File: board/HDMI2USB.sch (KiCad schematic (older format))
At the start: 0 parts

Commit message: Issue #1481 - GPIO sheet
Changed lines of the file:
@@
 LIBS:valves
 LIBS:hdmi2usb
+LIBS:timvideos-pcie-8x
 LIBS:HDMI2USB-cache
-LIBS:Atlys-VHDCI-cache
 EELAYER 27 0
 EELAYER END
@@
 Sheet 1 12
 Title "HDMI2USB"
-Date "18 feb 2015"
+Date "20 feb 2015"
 Rev "Rev2"
 Comp ""
@@
 F38 "USB_RESETB" B R 5700 5950 60
 F39 "USB_REFCLK" B R 5700 5850 60
-$EndSheet
-$Sheet
-S 6550 1100 2000 2400
-U 54886DFB
-F0 "Ethernet" 50
-F1 "Ethernet.sch" 50
-F2 "ETH_TXD[0..3]" I R 8550 1500 60
-F3 "ETH_TXCTL" I R 8550 1700 60
-F4 "ETH_RXD[0..3]" I R 8550 1600 60
-F5 "ETH_TXCLK" I R 8550 1800 60
-F6 "ETH_RXCTL" I R 8550 1900 60
-F7 "ETH_RXCLK" I R 8550 2000 60
-F8 "ETH_INT_B" I R 8550 2100 60
-F9 "ETH_RESET_B" I R 8550 2200 60
-F10 "SYSCLK" I R 8550 2300 60
-F11 "FPGA_CLK" I R 8550 2400 60
-F12 "ETH_MDC" I R 8550 2500 60
-F13 "MAC_SCL" I R 8550 2800 60
-F14 "ETH_MDIO" I R 8550 2600 60
-F15 "MAC_SDA" I R 8550 2700 60
 $EndSheet
 $Sheet
@@
 	8550 2200 9800 2200
 Wire Wire Line
-	8550 2300 9800 2300
-Wire Wire Line
 	8550 2400 9800 2400
 Wire Wire Line
@@
 Wire Wire Line
 	8550 2600 9800 2600
-Wire Wire Line
-	8550 2700 9800 2700
 Wire Bus Line
 	3400 4300 3750 4300
@@
 Wire Bus Line
 	8550 4150 9800 4150
+$Sheet
+S 6550 1100 2000 2400
+U 54886DFB
+F0 "Ethernet" 50
+F1 "Ethernet.sch" 50
+F2 "ETH_TXD[0..3]" O R 8550 1500 60
+F3 "ETH_TXCTL" O R 8550 1700 60
+F4 "ETH_RXD[0..3]" I R 8550 1600 60
+F5 "ETH_TXCLK" O R 8550 1800 60
+F6 "ETH_RXCTL" I R 8550 1900 60
+F7 "ETH_RXCLK" I R 8550 2000 60
+F8 "ETH_INT_B" I R 8550 2100 60
+F9 "ETH_RESET_B" I R 8550 2200 60
+F10 "FPGA_CLK" I R 8550 2400 60
+F11 "ETH_MDC" I R 8550 2500 60
+F12 "MAC_SCL" I R 8550 2700 60
+F13 "ETH_MDIO" B R 8550 2600 60
+F14 "MAC_SDA" B R 8550 2800 60
+$EndSheet
 $Sheet
 S 9800 1100 2050 8900
@@
 F68 "CYPRESS-RESET" B L 9800 6400 60
 F69 "GTP_CLK" O L 9800 6500 60
-F70 "RX_CLK" O L 9800 3150 60
-F71 "ETH_RXCTL" I L 9800 1900 60
-F72 "ETH_RXCLK" I L 9800 2000 60
-F73 "ETH_RXD[0..3]" I L 9800 1600 60
-F74 "ETH_MDC" I L 9800 2500 60
-F75 "ETH_MDIO" I L 9800 2600 60
-F76 "ETH_RESET_B" I L 9800 2200 60
-F77 "ETH_INT_B" I L 9800 2100 60
-F78 "ETH_TXCLK" I L 9800 1800 60
-F79 "ETH_TXCTL" I L 9800 1700 60
-F80 "ETH_TXD[0..3]" I L 9800 1500 60
-F81 "FPGA_CLK" I L 9800 2400 60
-F82 "MAC_SCL" I L 9800 2800 60
-F83 "MAC_SDA" I L 9800 2700 60
-F84 "SYSCLK" I L 9800 2300 60
-$EndSheet
-$Sheet
-S 1900 7250 1450 2350
+F70 "ETH_RXCTL" O L 9800 1900 60
+F71 "ETH_RXCLK" O L 9800 2000 60
+F72 "ETH_RXD[0..3]" O L 9800 1600 60
+F73 "ETH_MDC" O L 9800 2500 60
+F74 "ETH_MDIO" B L 9800 2600 60
+F75 "ETH_RESET_B" O L 9800 2200 60
+F76 "ETH_INT_B" O L 9800 2100 60
+F77 "ETH_TXCLK" I L 9800 1800 60
+F78 "ETH_TXCTL" I L 9800 1700 60
+F79 "ETH_TXD[0..3]" I L 9800 1500 60
+F80 "FPGA_CLK" O L 9800 2400 60
+F81 "MAC_SCL" I L 9800 2700 60
+F82 "MAC_SDA" B L 9800 2800 60
+$EndSheet
+Wire Wire Line
+	9800 2800 8550 2800
+Wire Wire Line
+	8550 2700 9800 2700
+$Sheet
+S 1950 7250 1650 3400
 U 54E594A7
 F0 "GPIOs" 50
 F1 "GPIOs.sch" 50
+F2 "DIFFIO_A1N" B R 3600 7650 60
+F3 "DIFFIO_A2N" B R 3600 7850 60
+F4 "DIFFIO_A3N" B R 3600 8050 60
+F5 "DIFFCLK_A0N" B R 3600 9050 60
+F6 "DIFFIO_A4N" B R 3600 8250 60
+F7 "DIFFIO_A5N" B R 3600 8450 60
+F8 "DIFFIO_A6N" B R 3600 8650 60
+F9 "DIFFCLK_A1N" B R 3600 9300 60
+F10 "DIFFIO_B1N" B L 1950 7650 60
+F11 "DIFFIO_B2N" B L 1950 7850 60
+F12 "DIFFIO_B3N" B L 1950 8050 60
+F13 "DIFFCLK_B0N" B L 1950 9050 60
+F14 "DIFFIO_B4N" B L 1950 8250 60
+F15 "DIFFIO_B0N" B L 1950 7450 60
+F16 "DIFFIO_B6N" B L 1950 8650 60
+F17 "DIFFCLK_B1N" I L 1950 9300 60
+F18 "DIFFCLK_A1P" I R 3600 8950 60
+F19 "DIFFIO_A1P" B R 3600 7550 60
+F20 "DIFFIO_A2P" B R 3600 7750 60
+F21 "DIFFIO_A3P" B R 3600 7950 60
+F22 "DIFFCLK_A0P" B R 3600 9200 60
+F23 "DIFFIO_A4P" B R 3600 8150 60
+F24 "DIFFIO_A5P" B R 3600 8350 60
+F25 "DIFFIO_A6P" B R 3600 8550 60
+F26 "DIFFIO_B1P" B L 1950 7550 60
+F27 "DIFFIO_B2P" B L 1950 7750 60
+F28 "DIFFIO_B3P" B L 1950 7950 60
+F29 "DIFFCLK_B0P" B L 1950 8950 60
+F30 "DIFFIO_B4P" B L 1950 8150 60
+F31 "DIFFIO_B5P" B L 1950 8350 60
+F32 "DIFFIO_B6P" B L 1950 8550 60
+F33 "DIFFCLK_B1P" I L 1950 9200 60
+F34 "SMCLK" I L 1950 9450 60
+F35 "SMDATA" B L 1950 9550 60
+F36 "PCIE_RESET" I L 1950 9650 60
+F37 "DIFFIO_XP" B R 3600 9550 60
+F38 "DIFFIO_XN" B R 3600 9650 60
+F39 "DIFFIO_YN" B R 3600 9850 60
+F40 "DIFFIO_YP" B R 3600 9750 60
+F41 "DIFFCLK_XN" B R 3600 10250 60
+F42 "DIFFCLK_XP" B R 3600 10150 60
+F43 "DIFFIO_A0N" B R 3600 7450 60
+F44 "DIFFIO_A0P" B R 3600 7350 60
+F45 "DIFFIO_B0P" B L 1950 7350 60
+F46 "DIFFIO_ZN" B R 3600 10050 60
+F47 "DIFFIO_ZP" B R 3600 9950 60
+F48 "GPIO[0..15]" B L 1950 9900 60
+F49 "DIFFIO_B5N" B L 1950 8450 60
 $EndSheet
 $EndSCHEMATC

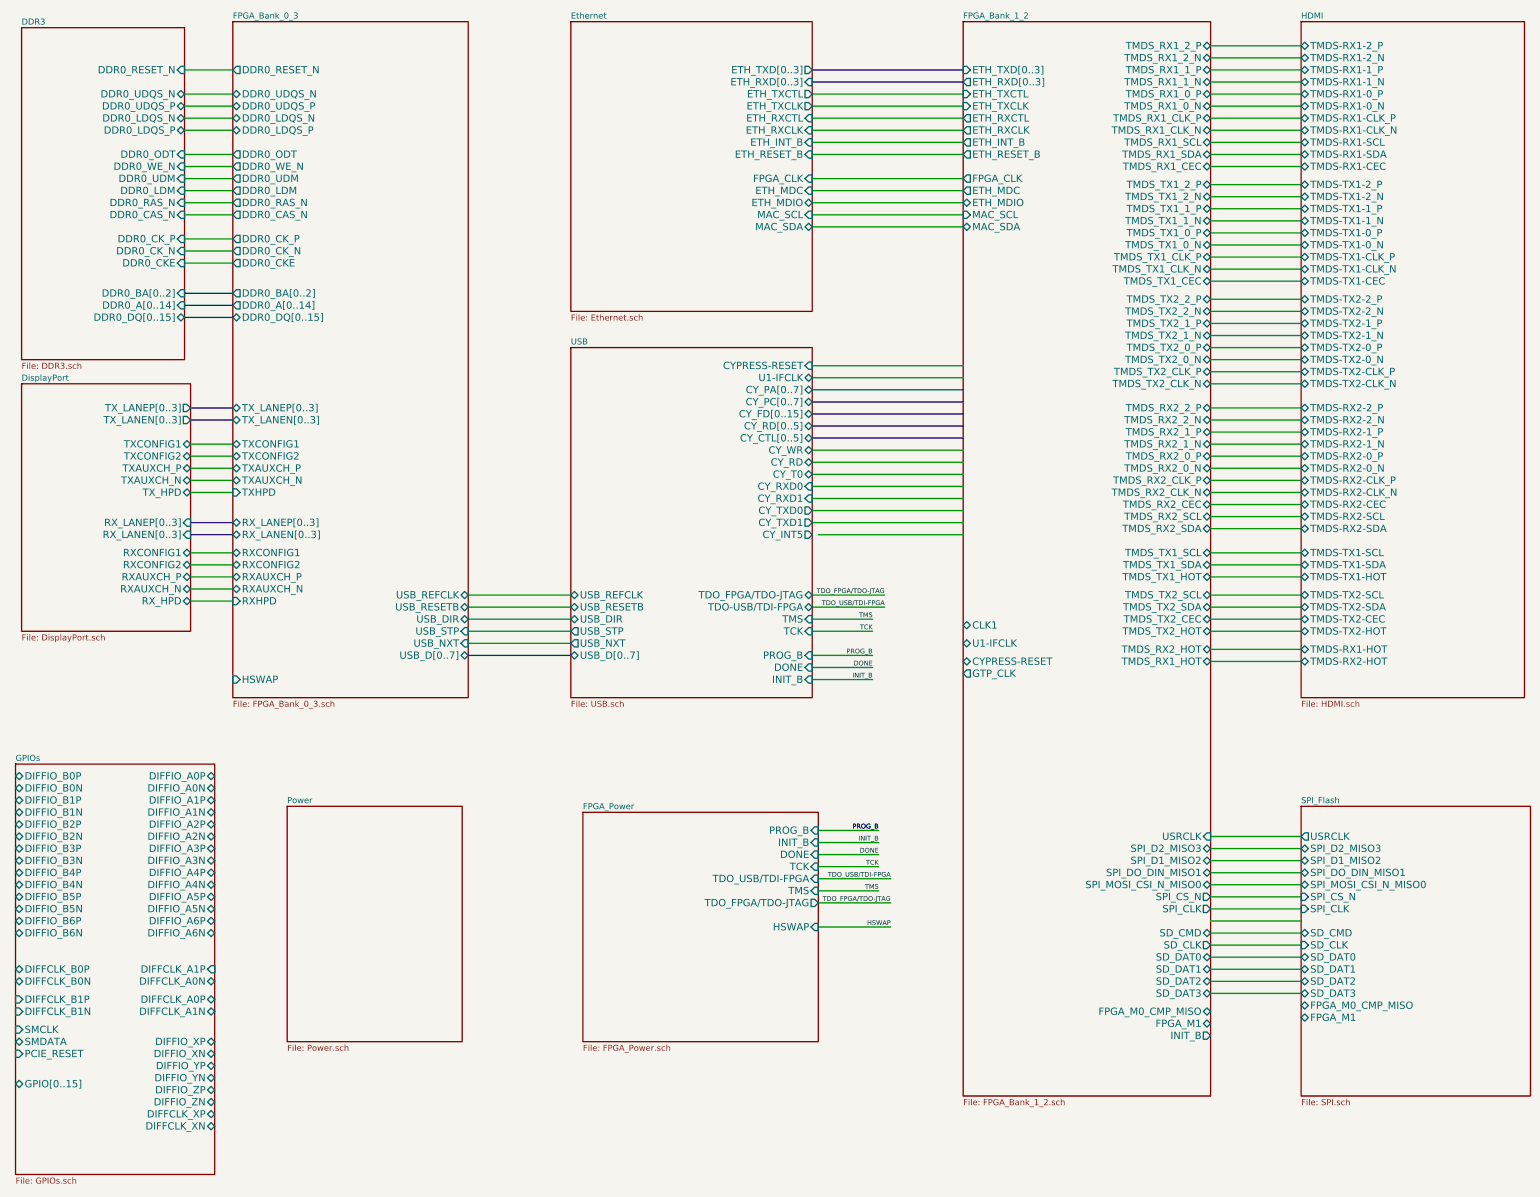
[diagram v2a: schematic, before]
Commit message: Issue #1481 - CYPRESS-FPGA CONNECTIONS ADDED
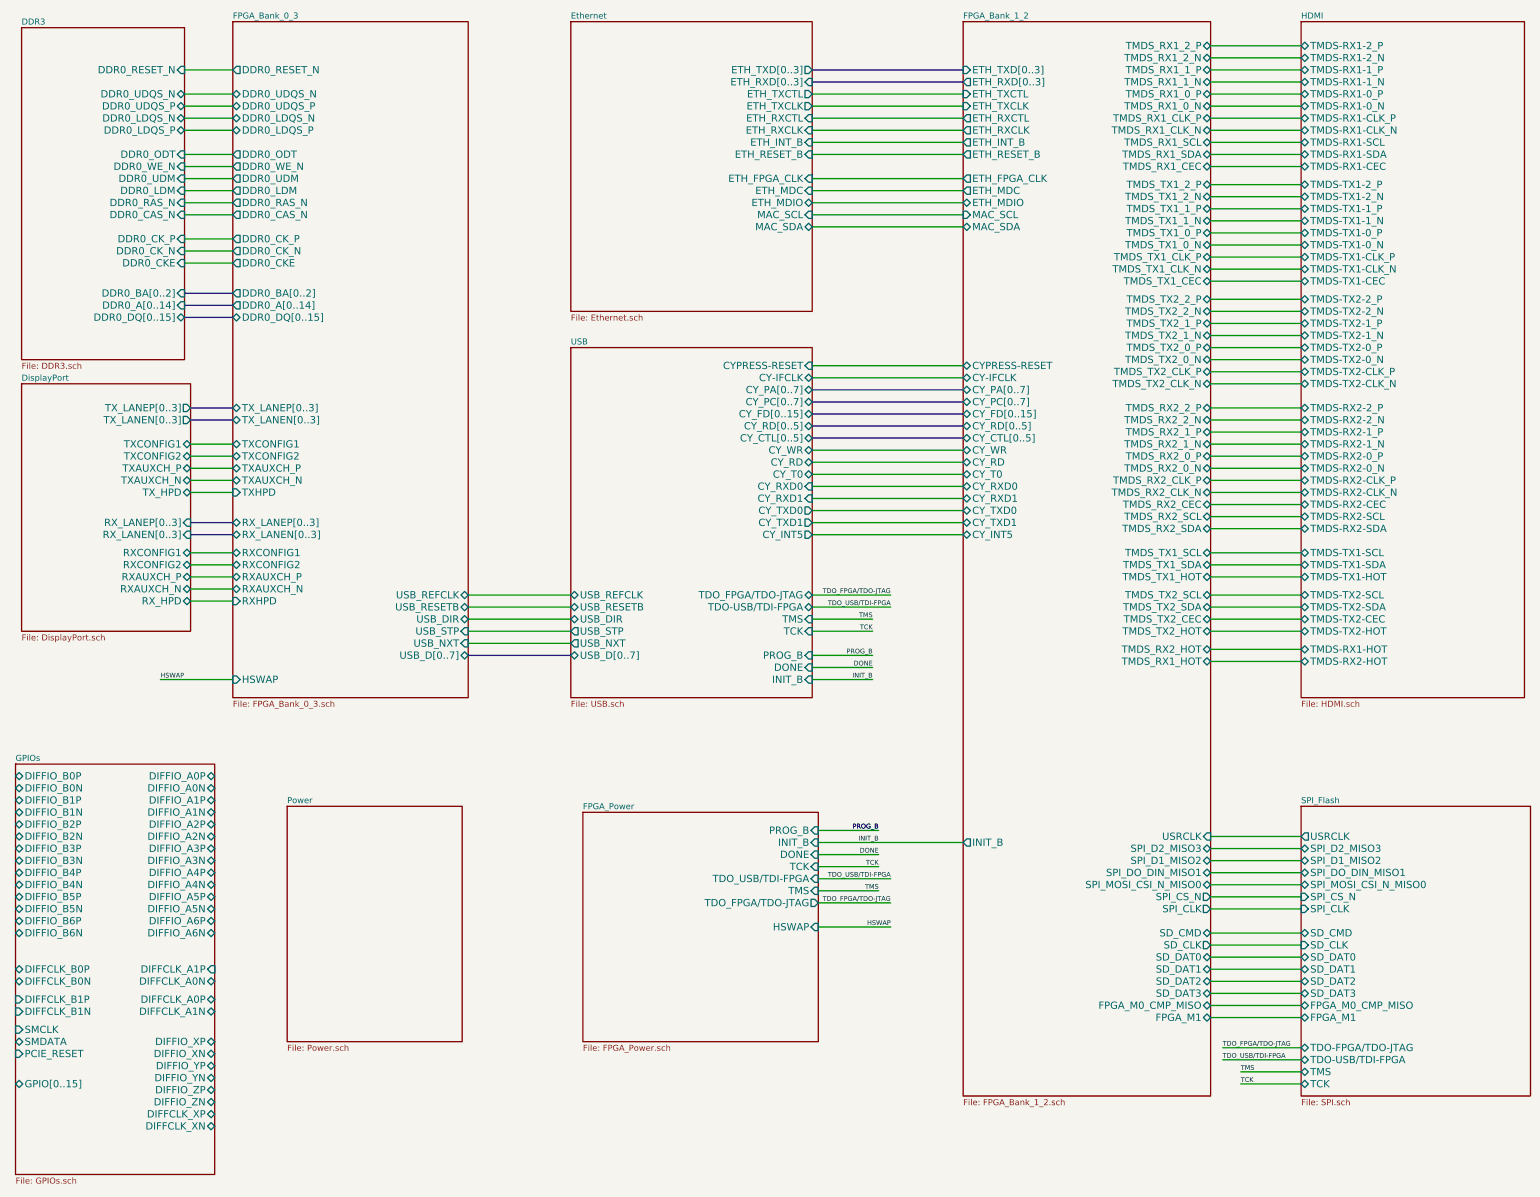
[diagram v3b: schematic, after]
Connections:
- wire segments 127 -> 133
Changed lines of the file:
@@
 Sheet 1 12
 Title "HDMI2USB"
-Date "20 feb 2015"
+Date "24 feb 2015"
 Rev "Rev2"
 Comp ""
@@
 Text Label 9050 6150 2    39   ~ 0
 TCK
-Text Label 9150 5950 2    39   ~ 0
+Text Label 9200 5950 2    39   ~ 0
 TDO_USB/TDI-FPGA
-Text Label 9150 5850 2    39   ~ 0
+Text Label 9200 5850 2    39   ~ 0
 TDO_FPGA/TDO-JTAG
 Text Label 9050 6050 2    39   ~ 0
@@
 F15 "SD_DAT2" B L 12600 9050 60
 F16 "USRCLK" O L 12600 7850 60
+F17 "TDO-USB/TDI-FPGA" B L 12600 9700 60
+F18 "TDO-FPGA/TDO-JTAG" B L 12600 9600 60
+F19 "TCK" B L 12600 9900 60
+F20 "TMS" B L 12600 9800 60
 $EndSheet
 $Sheet
@@
 F14 "USB_RESETB" B L 6550 5950 60
 F15 "USB_REFCLK" B L 6550 5850 60
-F16 "U1-IFCLK" B R 8550 4050 60
+F16 "CY-IFCLK" B R 8550 4050 60
 F17 "CY_PA[0..7]" B R 8550 4150 60
 F18 "CY_PC[0..7]" B R 8550 4250 60
@@
 	11850 8450 12600 8450
 Wire Wire Line
-	11850 8550 12600 8550
-Wire Wire Line
 	11850 8650 12600 8650
 Wire Wire Line
@@
 	8600 7800 9100 7800
 Wire Wire Line
-	8600 7900 9100 7900
+	8600 7900 9800 7900
 Wire Wire Line
 	8600 8100 9100 8100
@@
 	8550 6150 9050 6150
 Wire Wire Line
-	8550 5950 9150 5950
-Wire Wire Line
-	8550 5850 9150 5850
+	8550 5950 9200 5950
+Wire Wire Line
+	8550 5850 9200 5850
 Wire Wire Line
 	8550 6450 9050 6450
@@
 	8550 5050 9800 5050
 Wire Wire Line
-	8600 5350 9800 5350
+	8550 5350 9800 5350
 Wire Bus Line
 	8550 4550 9800 4550
@@
 Wire Bus Line
 	8550 4150 9800 4150
+Wire Wire Line
+	9800 2800 8550 2800
+Wire Wire Line
+	8550 2700 9800 2700
+$Sheet
+S 1950 7250 1650 3400
+U 54E594A7
+F0 "GPIOs" 50
+F1 "GPIOs.sch" 50
+F2 "DIFFIO_A1N" B R 3600 7650 60
+F3 "DIFFIO_A2N" B R 3600 7850 60
+F4 "DIFFIO_A3N" B R 3600 8050 60
+F5 "DIFFCLK_A0N" B R 3600 9050 60
+F6 "DIFFIO_A4N" B R 3600 8250 60
+F7 "DIFFIO_A5N" B R 3600 8450 60
+F8 "DIFFIO_A6N" B R 3600 8650 60
+F9 "DIFFCLK_A1N" B R 3600 9300 60
+F10 "DIFFIO_B1N" B L 1950 7650 60
+F11 "DIFFIO_B2N" B L 1950 7850 60
+F12 "DIFFIO_B3N" B L 1950 8050 60
+F13 "DIFFCLK_B0N" B L 1950 9050 60
+F14 "DIFFIO_B4N" B L 1950 8250 60
+F15 "DIFFIO_B0N" B L 1950 7450 60
+F16 "DIFFIO_B6N" B L 1950 8650 60
+F17 "DIFFCLK_B1N" I L 1950 9300 60
+F18 "DIFFCLK_A1P" I R 3600 8950 60
+F19 "DIFFIO_A1P" B R 3600 7550 60
+F20 "DIFFIO_A2P" B R 3600 7750 60
+F21 "DIFFIO_A3P" B R 3600 7950 60
+F22 "DIFFCLK_A0P" B R 3600 9200 60
+F23 "DIFFIO_A4P" B R 3600 8150 60
+F24 "DIFFIO_A5P" B R 3600 8350 60
+F25 "DIFFIO_A6P" B R 3600 8550 60
+F26 "DIFFIO_B1P" B L 1950 7550 60
+F27 "DIFFIO_B2P" B L 1950 7750 60
+F28 "DIFFIO_B3P" B L 1950 7950 60
+F29 "DIFFCLK_B0P" B L 1950 8950 60
+F30 "DIFFIO_B4P" B L 1950 8150 60
+F31 "DIFFIO_B5P" B L 1950 8350 60
+F32 "DIFFIO_B6P" B L 1950 8550 60
+F33 "DIFFCLK_B1P" I L 1950 9200 60
+F34 "SMCLK" I L 1950 9450 60
+F35 "SMDATA" B L 1950 9550 60
+F36 "PCIE_RESET" I L 1950 9650 60
+F37 "DIFFIO_XP" B R 3600 9550 60
+F38 "DIFFIO_XN" B R 3600 9650 60
+F39 "DIFFIO_YN" B R 3600 9850 60
+F40 "DIFFIO_YP" B R 3600 9750 60
+F41 "DIFFCLK_XN" B R 3600 10250 60
+F42 "DIFFCLK_XP" B R 3600 10150 60
+F43 "DIFFIO_A0N" B R 3600 7450 60
+F44 "DIFFIO_A0P" B R 3600 7350 60
+F45 "DIFFIO_B0P" B L 1950 7350 60
+F46 "DIFFIO_ZN" B R 3600 10050 60
+F47 "DIFFIO_ZP" B R 3600 9950 60
+F48 "GPIO[0..15]" B L 1950 9900 60
+F49 "DIFFIO_B5N" B L 1950 8450 60
+$EndSheet
 $Sheet
 S 6550 1100 2000 2400
@@
 F8 "ETH_INT_B" I R 8550 2100 60
 F9 "ETH_RESET_B" I R 8550 2200 60
-F10 "FPGA_CLK" I R 8550 2400 60
-F11 "ETH_MDC" I R 8550 2500 60
-F12 "MAC_SCL" I R 8550 2700 60
-F13 "ETH_MDIO" B R 8550 2600 60
-F14 "MAC_SDA" B R 8550 2800 60
+F10 "ETH_MDC" I R 8550 2500 60
+F11 "MAC_SCL" I R 8550 2700 60
+F12 "ETH_MDIO" B R 8550 2600 60
+F13 "MAC_SDA" B R 8550 2800 60
+F14 "ETH_FPGA_CLK" I R 8550 2400 60
 $EndSheet
 $Sheet
@@
 F0 "FPGA_Bank_1_2" 50
 F1 "FPGA_Bank_1_2.sch" 50
-F2 "FPGA_M0_CMP_MISO" B R 11850 9300 60
+F2 "FPGA_M0_CMP_MISO" B R 11850 9250 60
 F3 "SPI_D1_MISO2" B R 11850 8050 60
 F4 "SPI_DO_DIN_MISO1" B R 11850 8150 60
@@
 F7 "SPI_MOSI_CSI_N_MISO0" B R 11850 8250 60
 F8 "SPI_D2_MISO3" B R 11850 7950 60
-F9 "FPGA_M1" B R 11850 9400 60
-F10 "INIT_B" O R 11850 9500 60
+F9 "FPGA_M1" B R 11850 9350 60
+F10 "INIT_B" O L 9800 7900 60
 F11 "SD_DAT0" B R 11850 8850 60
 F12 "SD_DAT1" B R 11850 8950 60
@@
 F64 "TMDS_TX1_2_N" B R 11850 2550 60
 F65 "TMDS_TX2_2_N" B R 11850 3500 60
-F66 "CLK1" B L 9800 6100 60
-F67 "U1-IFCLK" B L 9800 6250 60
-F68 "CYPRESS-RESET" B L 9800 6400 60
-F69 "GTP_CLK" O L 9800 6500 60
-F70 "ETH_RXCTL" O L 9800 1900 60
-F71 "ETH_RXCLK" O L 9800 2000 60
-F72 "ETH_RXD[0..3]" O L 9800 1600 60
-F73 "ETH_MDC" O L 9800 2500 60
-F74 "ETH_MDIO" B L 9800 2600 60
-F75 "ETH_RESET_B" O L 9800 2200 60
-F76 "ETH_INT_B" O L 9800 2100 60
-F77 "ETH_TXCLK" I L 9800 1800 60
-F78 "ETH_TXCTL" I L 9800 1700 60
-F79 "ETH_TXD[0..3]" I L 9800 1500 60
-F80 "FPGA_CLK" O L 9800 2400 60
-F81 "MAC_SCL" I L 9800 2700 60
-F82 "MAC_SDA" B L 9800 2800 60
-$EndSheet
-Wire Wire Line
-	9800 2800 8550 2800
-Wire Wire Line
-	8550 2700 9800 2700
-$Sheet
-S 1950 7250 1650 3400
-U 54E594A7
-F0 "GPIOs" 50
-F1 "GPIOs.sch" 50
-F2 "DIFFIO_A1N" B R 3600 7650 60
-F3 "DIFFIO_A2N" B R 3600 7850 60
-F4 "DIFFIO_A3N" B R 3600 8050 60
-F5 "DIFFCLK_A0N" B R 3600 9050 60
-F6 "DIFFIO_A4N" B R 3600 8250 60
-F7 "DIFFIO_A5N" B R 3600 8450 60
-F8 "DIFFIO_A6N" B R 3600 8650 60
-F9 "DIFFCLK_A1N" B R 3600 9300 60
-F10 "DIFFIO_B1N" B L 1950 7650 60
-F11 "DIFFIO_B2N" B L 1950 7850 60
-F12 "DIFFIO_B3N" B L 1950 8050 60
-F13 "DIFFCLK_B0N" B L 1950 9050 60
-F14 "DIFFIO_B4N" B L 1950 8250 60
-F15 "DIFFIO_B0N" B L 1950 7450 60
-F16 "DIFFIO_B6N" B L 1950 8650 60
-F17 "DIFFCLK_B1N" I L 1950 9300 60
-F18 "DIFFCLK_A1P" I R 3600 8950 60
-F19 "DIFFIO_A1P" B R 3600 7550 60
-F20 "DIFFIO_A2P" B R 3600 7750 60
-F21 "DIFFIO_A3P" B R 3600 7950 60
-F22 "DIFFCLK_A0P" B R 3600 9200 60
-F23 "DIFFIO_A4P" B R 3600 8150 60
-F24 "DIFFIO_A5P" B R 3600 8350 60
-F25 "DIFFIO_A6P" B R 3600 8550 60
-F26 "DIFFIO_B1P" B L 1950 7550 60
-F27 "DIFFIO_B2P" B L 1950 7750 60
-F28 "DIFFIO_B3P" B L 1950 7950 60
-F29 "DIFFCLK_B0P" B L 1950 8950 60
-F30 "DIFFIO_B4P" B L 1950 8150 60
-F31 "DIFFIO_B5P" B L 1950 8350 60
-F32 "DIFFIO_B6P" B L 1950 8550 60
-F33 "DIFFCLK_B1P" I L 1950 9200 60
-F34 "SMCLK" I L 1950 9450 60
-F35 "SMDATA" B L 1950 9550 60
-F36 "PCIE_RESET" I L 1950 9650 60
-F37 "DIFFIO_XP" B R 3600 9550 60
-F38 "DIFFIO_XN" B R 3600 9650 60
-F39 "DIFFIO_YN" B R 3600 9850 60
-F40 "DIFFIO_YP" B R 3600 9750 60
-F41 "DIFFCLK_XN" B R 3600 10250 60
-F42 "DIFFCLK_XP" B R 3600 10150 60
-F43 "DIFFIO_A0N" B R 3600 7450 60
-F44 "DIFFIO_A0P" B R 3600 7350 60
-F45 "DIFFIO_B0P" B L 1950 7350 60
-F46 "DIFFIO_ZN" B R 3600 10050 60
-F47 "DIFFIO_ZP" B R 3600 9950 60
-F48 "GPIO[0..15]" B L 1950 9900 60
-F49 "DIFFIO_B5N" B L 1950 8450 60
-$EndSheet
+F66 "ETH_RXCTL" O L 9800 1900 60
+F67 "ETH_RXCLK" O L 9800 2000 60
+F68 "ETH_RXD[0..3]" O L 9800 1600 60
+F69 "ETH_MDC" O L 9800 2500 60
+F70 "ETH_MDIO" B L 9800 2600 60
+F71 "ETH_RESET_B" O L 9800 2200 60
+F72 "ETH_INT_B" O L 9800 2100 60
+F73 "ETH_TXCLK" I L 9800 1800 60
+F74 "ETH_TXCTL" I L 9800 1700 60
+F75 "ETH_TXD[0..3]" I L 9800 1500 60
+F76 "ETH_FPGA_CLK" O L 9800 2400 60
+F77 "MAC_SCL" I L 9800 2700 60
+F78 "MAC_SDA" B L 9800 2800 60
+F79 "CYPRESS-RESET" B L 9800 3950 60
+F80 "CY-IFCLK" B L 9800 4050 60
+F81 "CY_PA[0..7]" B L 9800 4150 60
+F82 "CY_FD[0..15]" B L 9800 4350 60
+F83 "CY_PC[0..7]" B L 9800 4250 60
+F84 "CY_RD[0..5]" B L 9800 4450 60
+F85 "CY_CTL[0..5]" B L 9800 4550 60
+F86 "CY_RD" B L 9800 4750 60
+F87 "CY_WR" B L 9800 4650 60
+F88 "CY_T0" B L 9800 4850 60
+F89 "CY_RXD0" B L 9800 4950 60
+F90 "CY_RXD1" B L 9800 5050 60
+F91 "CY_TXD0" B L 9800 5150 60
+F92 "CY_TXD1" B L 9800 5250 60
+F93 "CY_INT5" B L 9800 5350 60
+$EndSheet
+Text Label 12100 9900 0    39   ~ 0
+TCK
+Text Label 11950 9700 0    39   ~ 0
+TDO_USB/TDI-FPGA
+Text Label 11950 9600 0    39   ~ 0
+TDO_FPGA/TDO-JTAG
+Text Label 12100 9800 0    39   ~ 0
+TMS
+Wire Wire Line
+	12600 9900 12100 9900
+Wire Wire Line
+	12600 9700 11950 9700
+Wire Wire Line
+	12600 9600 11950 9600
+Wire Wire Line
+	12100 9800 12600 9800
+Text Label 3150 6550 0    39   ~ 0
+HSWAP
+Wire Wire Line
+	3750 6550 3150 6550
+Wire Wire Line
+	11850 9250 12600 9250
+Wire Wire Line
+	11850 9350 12600 9350
 $EndSCHEMATC
